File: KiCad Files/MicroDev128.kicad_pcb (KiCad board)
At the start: 4 copper layers, 49.1 x 17.8 mm, 25 parts, among them J1 UPDI Header, J3 GPIO, J4 PWR and ANALOG, SW1 SW_SP3T, SW2 RST, U1 AVR128DB32x-xRXB, U2 LT8653SEV_PBF

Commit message: Updated PCB, fixed errors, and added more docs
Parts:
- removed G***: LOGO, LOGO
- moved C4 3.85 mm to (111.1, 62.6)
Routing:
- net +5V: track 113.4 -> 104.8 mm
- net GND: track 21.9 -> 20.9 mm, vias 29 -> 28
- added copper zone on B.Cu, net GND
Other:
- board text added: "A2"
- board text added: "A3"
- board text added: "A4"
- board text added: "A5"
- board text added: "A6"
- board text added: "A7"
- board text added: "C0"
- board text added: "C1"
- board text added: "C2"
- board text added: "C3"
- board text added: "F3"
- board text added: "F4"
- board text added: "F5"
- board text added: "Rev 1B"
- board text removed: "MicroDev"
- board text removed: "MicroDev128-32P"
- board text removed: "PA2"
- board text removed: "PA3"
- board text removed: "PA4"
- board text removed: "PA5"
- board text removed: "PA6"
- board text removed: "PA7"
- board text removed: "PC0"
- board text removed: "PC1"
- board text removed: "PC2"
- board text removed: "PC3"
- board text removed: "PF2"
- board text removed: "PF3"
- board text removed: "PF4"
- board text removed: "PF5"
- board text removed: "Rev 1A"

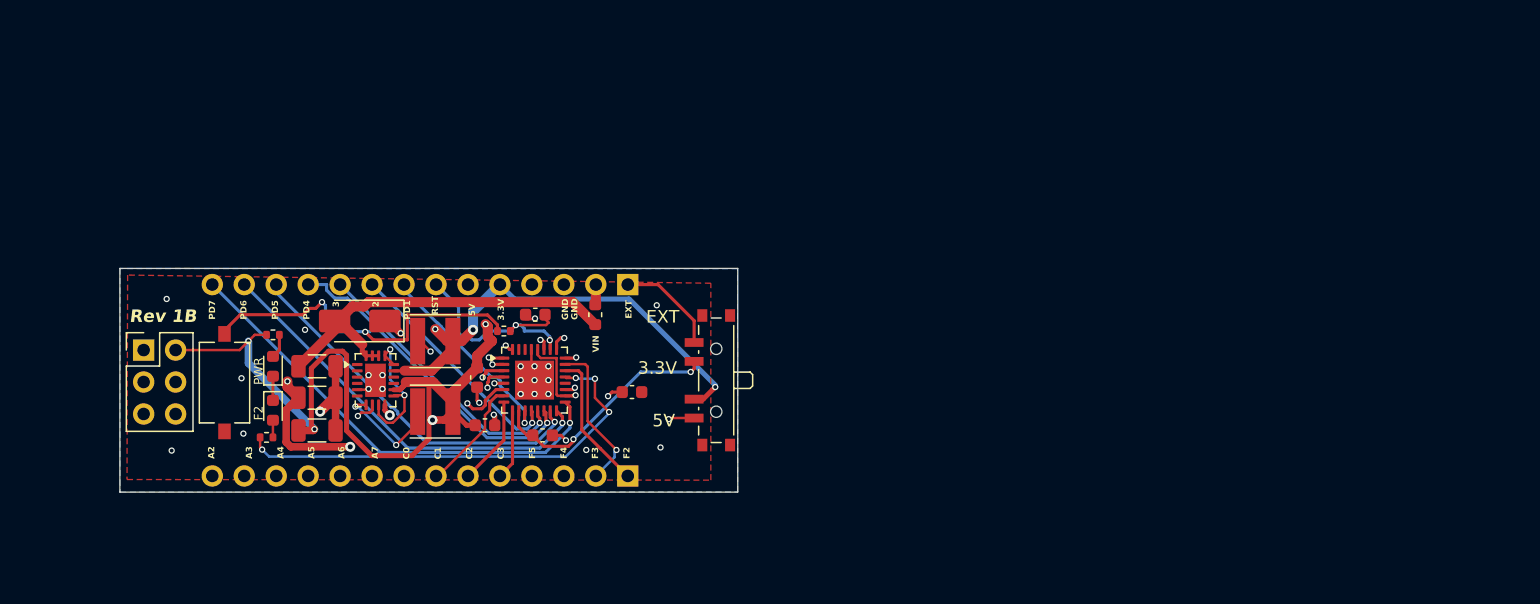
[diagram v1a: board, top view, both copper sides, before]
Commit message: Updated Naming, and started in dev work
On rev 1B
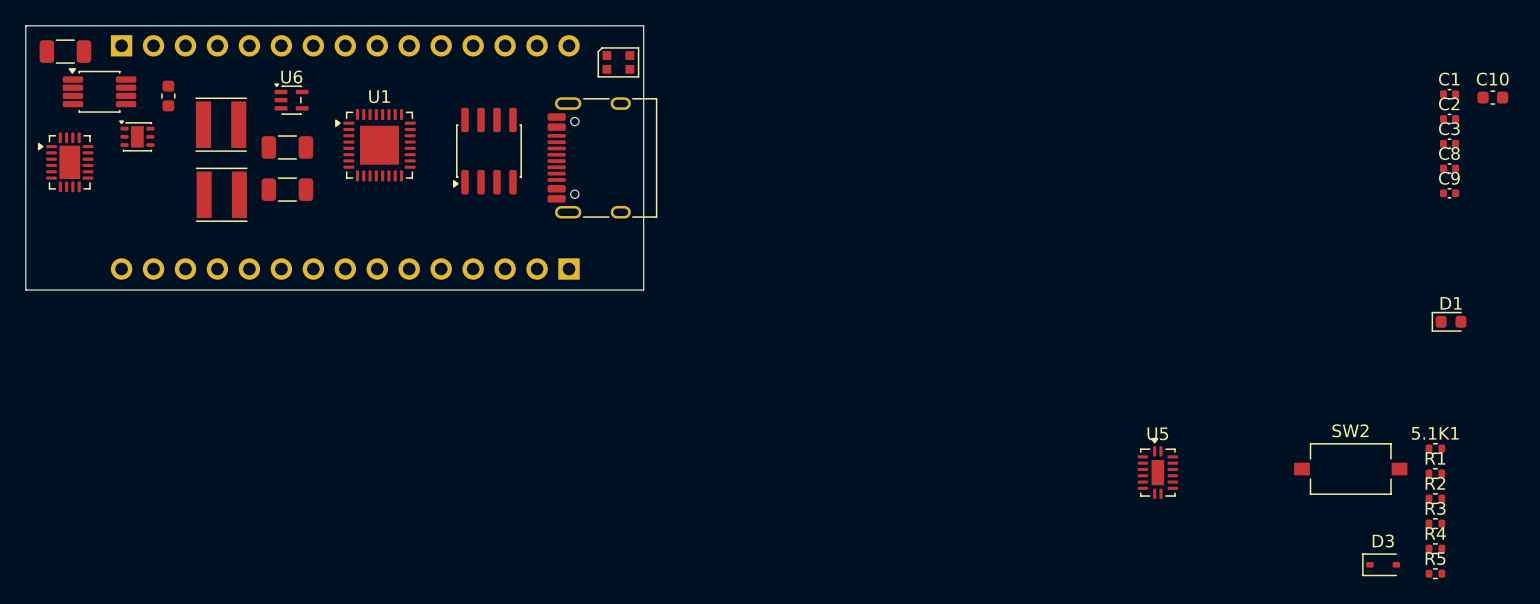
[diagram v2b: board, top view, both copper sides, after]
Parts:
- removed C4: 1uf, Capacitor_SMD:C_0603_1608Metric
- removed J4: PWR and ANALOG, Connector_PinHeader_2.54mm:PinHeader_1x14_P2.54mm_Vertical
- removed SW1: SW_SP3T, Button_Switch_SMD:SW_SP3T_PCM13
- added 5.1K1: R, Resistor_SMD:R_0402_1005Metric, F.Cu at (175.0, 67.1)
- added C8: 2.2uF, Capacitor_SMD:C_0402_1005Metric, F.Cu at (176.1, 44.9)
- added C9: 100nF, Capacitor_SMD:C_0402_1005Metric, F.Cu at (176.1, 46.9)
- added J2: USB Connector, Connector_USB:USB_C_Receptacle_HRO_TYPE-C-31-M-12, F.Cu at (109.2, 44.0)
- added Q1: DMN6040FDE, Package_DFN_QFN:DFN-6-1EP_2x2mm_P0.65mm_EP1.01x1.7mm, F.Cu at (71.8, 42.4)
- added R1: 5.1K, Resistor_SMD:R_0402_1005Metric, F.Cu at (175.0, 69.1)
- added R5: 330, Resistor_SMD:R_0402_1005Metric, F.Cu at (175.0, 77.1)
- added U3: LM74610QDGKTQ1, Package_SO:VSSOP-8_3x3mm_P0.65mm, F.Cu at (68.8, 38.8)
- added U4: CH330N, Package_SO:SOIC-8_3.9x4.9mm_P1.27mm, F.Cu at (99.8, 43.5)
- added U5: 74HC4051, Package_DFN_QFN:DHVQFN-16-1EP_2.5x3.5mm_P0.5mm_EP1x2mm, F.Cu at (152.9, 69.0)
- added U6: TLV70018_SOT353, Package_TO_SOT_SMD:SOT-353_SC-70-5, F.Cu at (84.1, 39.5)
- C1, C2: footprint Capacitor_SMD:C_0603_1608Metric -> Capacitor_SMD:C_0402_1005Metric
- C3: value 1uf -> 1uF; footprint Capacitor_SMD:C_0603_1608Metric -> Capacitor_SMD:C_0402_1005Metric
- D2: value L -> WS2812B-2020; footprint LED_SMD:LED_0603_1608Metric -> LED_SMD:LED_WS2812B-2020_PLCC4_2.0x2.0mm
- D3: value SMAJ36CA -> D; footprint Diode_SMD:D_SMA -> Diode_SMD:D_SOD-323
- J1: value UPDI Header -> Header 2; footprint Connector_PinHeader_2.54mm:PinHeader_2x03_P2.54mm_Vertical -> Connector_PinHeader_2.54mm:PinHeader_1x15_P2.54mm_Vertical; moved to B.Cu
- J3: value GPIO -> Header 1; footprint Connector_PinHeader_2.54mm:PinHeader_1x14_P2.54mm_Vertical -> Connector_PinHeader_2.54mm:PinHeader_1x15_P2.54mm_Vertical
- R3: value 330 -> 4.7K
- moved R4 93.9 mm to (175.0, 75.1)
- moved D1 93.7 mm to (176.2, 57.1), turned to 0 degrees
- moved R3 93.1 mm to (175.0, 73.1)
- moved SW2 89.8 mm to (168.3, 68.8), turned to 0 degrees
- moved D3 83.6 mm to (170.8, 76.4), turned to 0 degrees
- moved C1 80.5 mm to (176.1, 39.0), turned to 0 degrees
- moved C2 80.4 mm to (176.1, 40.9)
- moved C10 78.0 mm to (179.5, 39.2), turned to 0 degrees
- moved C3 75.7 mm to (176.1, 42.9), turned to 0 degrees
- moved R2 75.2 mm to (175.0, 71.1)
- moved J3 52.8 mm to (70.6, 35.1), turned to -90 degrees
- moved D2 39.0 mm to (110.1, 36.5), turned to 0 degrees
- moved F1 38.1 mm to (74.3, 39.1)
- moved J1 34.4 mm to (106.1, 52.9), turned to 90 degrees
- moved C5 32.0 mm to (66.1, 35.6)
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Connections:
- C10 pad 1: Net-(J4-Pin_7) -> /RST
- C3 pad 1: GND -> +1V8
- C3 pad 2: Net-(U1-VDDIO2) -> GND
- C5 pad 1: Net-(D3-A2) -> Net-(Q1-S)
- D2 pad 1: GND -> unconnected-(D2-DOUT-Pad1)
- D2 pad 2: Net-(D2-A) -> GND
- D3 pad 1: GND -> +5V
- D3 pad 2: Net-(D3-A2) -> Net-(D3-A)
- F1 pad 1: VDC -> /PWR
- F1 pad 2: Net-(D3-A2) -> Net-(Q1-D)
- J1 pad 1: Net-(J1-Pin_1) -> unconnected-(J1-Pin_1-Pad1)
- J1 pad 2: +5V -> /PF4
- J1 pad 3: unconnected-(J1-Pin_3-Pad3) -> /PF5
- J1 pad 4: unconnected-(J1-Pin_4-Pad4) -> Net-(J1-Pin_4)
- J1 pad 5: unconnected-(J1-Pin_5-Pad5) -> Net-(J1-Pin_5)
- J1 pad 6: GND -> Net-(J1-Pin_6)
- J3 pad 1: Net-(J3-Pin_1) -> /EXT
- J3 pad 2: Net-(J3-Pin_2) -> /PWR
- J3 pad 3: Net-(J3-Pin_3) -> GND
- J3 pad 4: Net-(J3-Pin_4) -> GND
- J3 pad 5: Net-(J3-Pin_5) -> +1V8
- J3 pad 6: Net-(J3-Pin_6) -> +3.3V
- J3 pad 7: Net-(J3-Pin_7) -> +5V
- J3 pad 8: Net-(J3-Pin_8) -> /RST
- R2 pad 2: Net-(J4-Pin_7) -> /RST
- R3 pad 1: Net-(U1-XTAL32K2/PF1) -> Net-(U4-TXD)
- R3 pad 2: Net-(D2-A) -> /UPDI
- U1 pad 1: Net-(J3-Pin_13) -> Net-(J1-Pin_12)
- U1 pad 10: Net-(U1-VDDIO2) -> /VDDIO2
- U1 pad 11: Net-(J4-Pin_8) -> Net-(J3-Pin_9)
- U1 pad 12: Net-(J4-Pin_9) -> Net-(J3-Pin_10)
- U1 pad 13: Net-(J4-Pin_10) -> Net-(J3-Pin_11)
- U1 pad 14: Net-(J4-Pin_11) -> Net-(J3-Pin_12)
- U1 pad 15: Net-(J4-Pin_12) -> Net-(J3-Pin_13)
- U1 pad 16: Net-(J4-Pin_13) -> Net-(J3-Pin_14)
- U1 pad 17: Net-(J4-Pin_14) -> Net-(J3-Pin_15)
- U1 pad 2: Net-(J3-Pin_12) -> Net-(J1-Pin_11)
- U1 pad 20: unconnected-(U1-XTAL32K1/PF0-Pad20) -> /LED
- U1 pad 21: Net-(U1-XTAL32K2/PF1) -> /S0
- U1 pad 22: Net-(J3-Pin_1) -> /S1
- U1 pad 23: Net-(J3-Pin_2) -> /S2
- U1 pad 24: Net-(J3-Pin_3) -> /PF4
- U1 pad 25: Net-(J3-Pin_4) -> /PF5
- U1 pad 26: Net-(J4-Pin_7) -> /RST
- U1 pad 27: Net-(J1-Pin_1) -> /UPDI
- U1 pad 3: Net-(J3-Pin_11) -> Net-(J1-Pin_10)
- U1 pad 30: unconnected-(U1-XTALHF1/PA0-Pad30) -> Net-(J1-Pin_15)
- U1 pad 31: unconnected-(U1-XTALHF2/PA1-Pad31) -> Net-(J1-Pin_14)
- U1 pad 32: Net-(J3-Pin_14) -> Net-(J1-Pin_13)
- U1 pad 4: Net-(J3-Pin_10) -> Net-(J1-Pin_9)
- U1 pad 5: Net-(J3-Pin_9) -> Net-(J1-Pin_8)
- U1 pad 6: Net-(J3-Pin_8) -> Net-(J1-Pin_7)
- U1 pad 7: Net-(J3-Pin_7) -> Net-(J1-Pin_6)
- U1 pad 8: Net-(J3-Pin_6) -> Net-(J1-Pin_5)
- U1 pad 9: Net-(J3-Pin_5) -> Net-(J1-Pin_4)
- U2 pad 18: Net-(D3-A2) -> Net-(Q1-S)
- U2 pad 19: Net-(D3-A2) -> Net-(Q1-S)
- U2 pad 20: Net-(D3-A2) -> Net-(Q1-S)
- U2 pad 5: GND -> Net-(U2-RT)
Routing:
- net +5V: track 104.8 -> 0.00 mm, vias 7 -> 0
- net +3.3V: track 66.9 -> 0.00 mm, vias 6 -> 0
- net Net-(J4-Pin_14): track 37.0 -> 0.00 mm, vias 1 -> 0
- net Net-(U1-XTAL32K2/PF1): track 36.0 -> 0.00 mm, vias 4 -> 0
- net Net-(J1-Pin_1): track 35.9 -> 0.00 mm, vias 1 -> 0
- net Net-(J4-Pin_13): track 32.8 -> 0.00 mm, vias 1 -> 0
- net Net-(D3-A2): track 31.3 -> 0.00 mm
- net Net-(J4-Pin_12): track 29.9 -> 0.00 mm, vias 1 -> 0
- net Net-(J3-Pin_14): track 29.7 -> 0.00 mm, vias 1 -> 0
- net Net-(R2-Pad1): track 28.0 -> 0.00 mm, vias 2 -> 0
- net Net-(J4-Pin_11): track 25.9 -> 0.00 mm, vias 1 -> 0
- net Net-(J3-Pin_13): track 24.6 -> 0.00 mm, vias 1 -> 0
- net Net-(J3-Pin_12): track 23.0 -> 0.00 mm, vias 1 -> 0
- net Net-(U2-SW2): track 22.6 -> 0.00 mm, vias 2 -> 0
- net Net-(J4-Pin_10): track 22.2 -> 0.00 mm, vias 1 -> 0
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- removed copper zone on In2.Cu, net +5V
- removed copper zone on B.Cu, net GND
- removed copper zone on F.Cu, net GND
- removed copper zone on In1.Cu, net GND
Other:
- board size 49.1 x 17.8 mm -> 49.1 x 21 mm
- board text removed: "2"
- board text removed: "3"
- board text removed: "3.3V"
- board text removed: "5V"
- board text removed: "A2"
- board text removed: "A3"
- board text removed: "A4"
- board text removed: "A5"
- board text removed: "A6"
- board text removed: "A7"
- board text removed: "C0"
- board text removed: "C1"
- board text removed: "C2"
- board text removed: "C3"
- board text removed: "D"
- board text removed: "EXT"
- board text removed: "F2"
- board text removed: "F3"
- board text removed: "F4"
- board text removed: "F5"
- board text removed: "GND"
- board text removed: "M"
- board text removed: "PD1"
- board text removed: "PD4"
- board text removed: "PD5"
- board text removed: "PD6"
- board text removed: "PD7"
- board text removed: "PWR"
- board text removed: "RST"
- board text removed: "Rev 1B"
- board text removed: "VIN"
